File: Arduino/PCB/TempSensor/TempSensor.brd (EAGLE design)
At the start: 32.7 x 32.4 mm, 24 parts, among them IC1 DS1820, J1 FTDI_DEVICE, J2 FTDI_DEVICE, U1 ATMEGA328-AU, X1 16Mhz

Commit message: base board
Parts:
- removed PWR1: IE0503D, xp_power:XP_DIP
- added C10, C4, C5, C6, C7, C8, C9: 100n, rcl:C0805
- added C11: 10n, rcl:C0805
- added D1: RB161M-20TR, Components:SOD123
- added D2: BAT54HT1G, Components:SOD323_ST
- added L1: VLCF4020, Components:VLCF4020
- added R10, R11, R13, R9: 4k7, rcl:R0805
- added R8: 10k, rcl:R0805
- added U$1: LM2736X, Components:SOT23-6L
- added U$3: XC6210, Components:SOT23-5
- U$2: value OLED_0.96_I2C -> OLED_0.96_I2CSWITCHPOWER
- moved JP5 1.42 mm to (58.4, 51.4)
- moved JP4 0.90 mm to (52.7, 51.4)
- moved JP6 0.71 mm to (44.1, 51.4)
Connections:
- removed net VCC: J2.P$5, LED1.A, SJ2.1, U$2.VCC, U1.18, U1.4, U1.6
- new net N$19: C4.2, D2.C, U$1.1
- new net N$25: R8.1, U$1.4
- new net N$26: C9.2, IC1.3, R11.1
- new net N$27: C10.2, IC1.2, R13.1
- new net N$29: C11.2, U$3.4
- new net VIN: JP6.2, R8.2, U$1.5
- new net VO: C5.2, D2.A, L1.P$2, R9.2, U$3.1, U$3.3
- net +3V3: now also C6.2, C7.2, C8.2, J2.P$5, LED1.A, R11.2, SJ2.1, U$2.GND, U$3.5, U1.18, U1.4, U1.6; no longer IC1.3, PWR1.+VOUT
- net GND: now also C10.1, C11.1, C5.1, C6.1, C7.1, C8.1, C9.1, D1.A, JP6.1, R10.1, U$1.2, U$2.VCC, U$3.2; no longer PWR1.-VOUT, U$2.GND
- net N$11: now also C4.1, D1.C, L1.P$1, U$1.6; no longer JP6.2, PWR1.+VIN
- net N$14: now also R10.2, R9.1, U$1.3; no longer JP6.1, PWR1.-VIN
- net N$6: now also R13.2; no longer IC1.2
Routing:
- net GND: track 85.6 -> 1.86 mm, vias 1 -> 0
- net VCC: track 63.6 -> 0.00 mm
- net +3V3: track 62.0 -> 0.00 mm, vias 1 -> 0
- net N$20: track 54.6 -> 0.00 mm
- net N$10: track 53.3 -> 0.00 mm, vias 1 -> 0
- net N$18: track 44.2 -> 0.00 mm
- net N$6: track 39.2 -> 0.00 mm, vias 1 -> 0
- net N$5: track 36.7 -> 0.00 mm
- net N$12: track 36.3 -> 0.00 mm, vias 1 -> 0
- net N$13: track 32.8 -> 0.00 mm, vias 1 -> 0
- net N$16: track 26.0 -> 0.00 mm, vias 1 -> 0
- net N$8: track 23.4 -> 0.00 mm, vias 1 -> 0
- net N$9: track 23.2 -> 0.00 mm, vias 1 -> 0
- net N$4: track 21.8 -> 0.00 mm
- net N$3: track 17.2 -> 0.00 mm
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
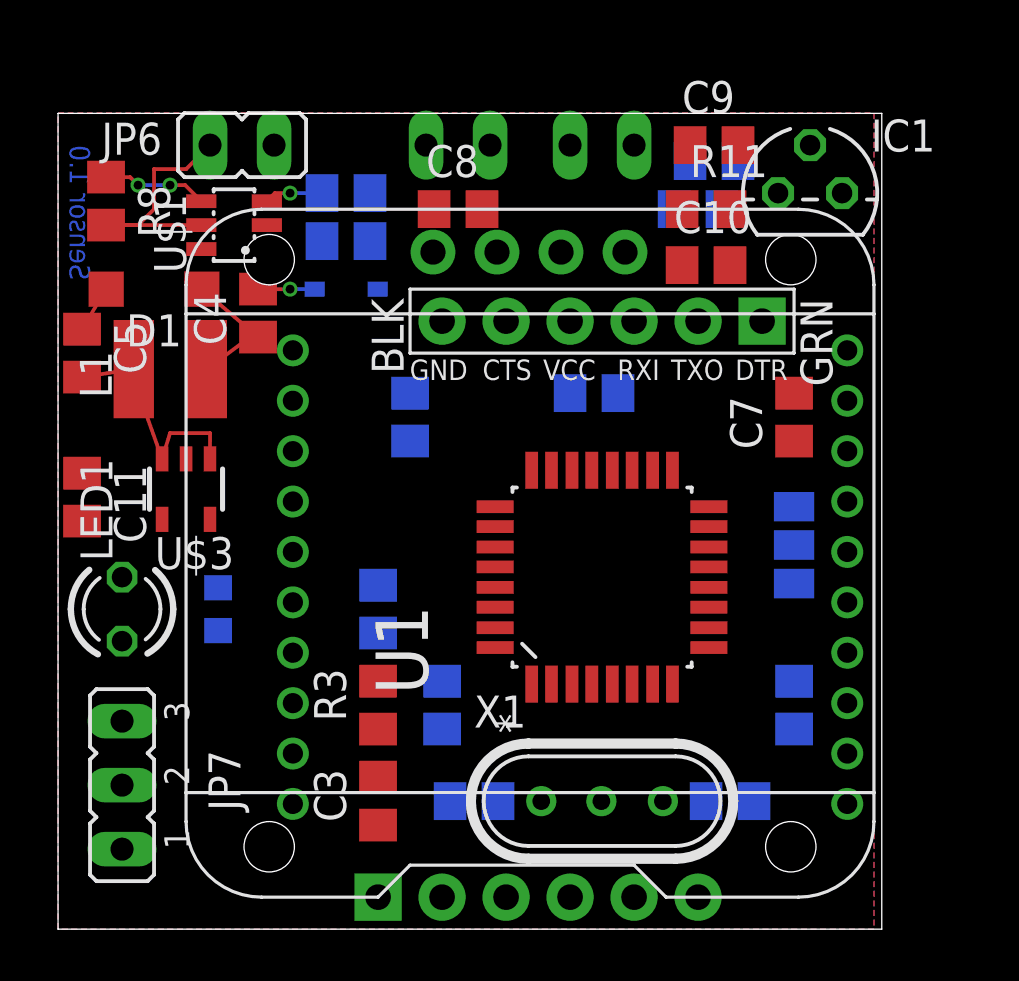
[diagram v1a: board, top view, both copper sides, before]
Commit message: Voor aanpassing board (verplaatsen toetsen en xbee)
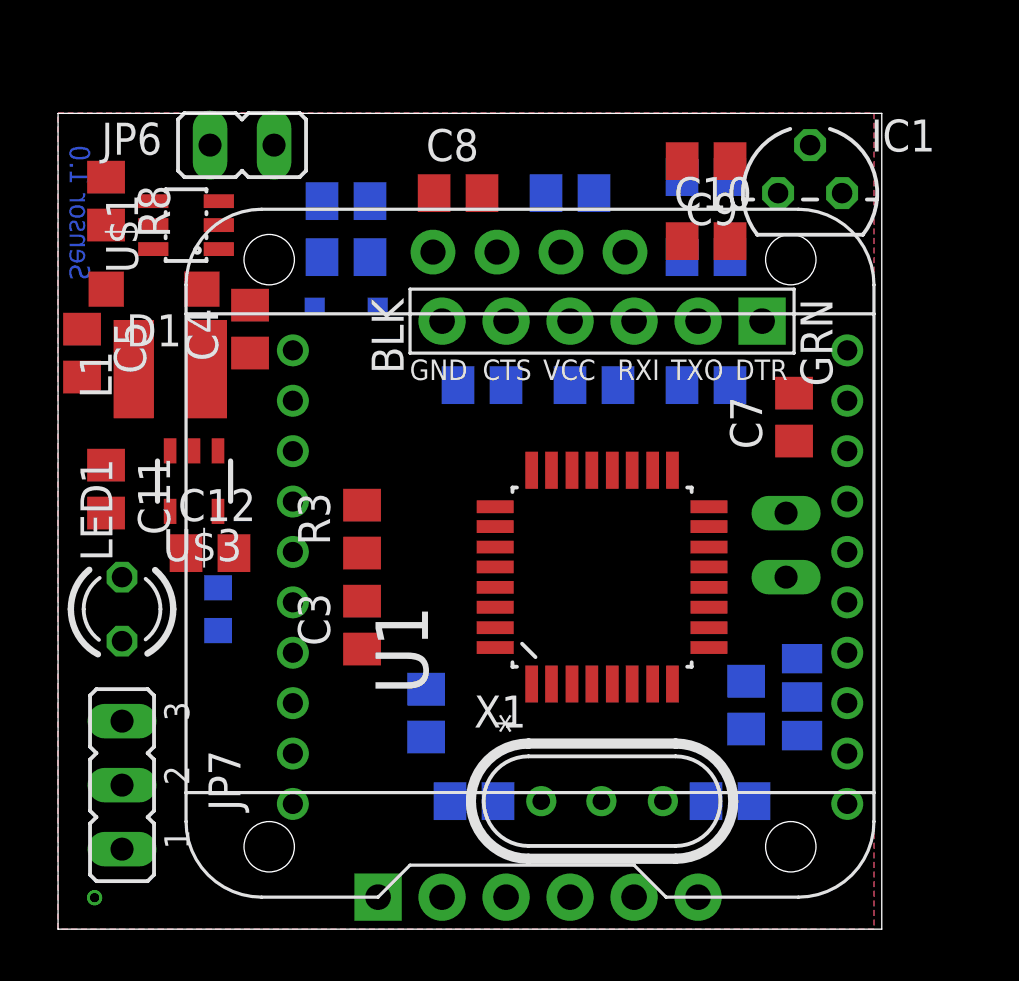
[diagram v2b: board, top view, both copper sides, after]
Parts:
- removed JP4: (no value), jumper:JP1
- added C12: 1u, rcl:C0805
- R10: value 4k7 -> 21K5
- R11, R13: value 4k7 -> 560
- R6, R7: value 4k7 -> 1M
- R9: value 4k7 -> 10K
- moved JP5 17.5 mm to (65.7, 35.6), turned to 180 degrees
- moved R1 15.8 mm to (62.5, 41.9), turned to 0 degrees
- moved R4 7.41 mm to (58.1, 41.9), turned to 0 degrees
- moved C3 7.01 mm to (48.9, 32.4)
- moved R3 7.01 mm to (48.9, 36.2)
- moved SJ2 6.04 mm to (66.4, 29.5)
- moved R5 5.12 mm to (57.1, 49.5), turned to 0 degrees
- moved C6 4.46 mm to (53.7, 41.9)
- moved R13 3.82 mm to (62.5, 47.0)
- moved R7 1.91 mm to (64.1, 29.2)
- moved U$1 1.91 mm to (41.9, 48.3)
- moved R11 1.27 mm to (62.5, 50.2), flipped to the bottom, turned to 180 degrees
- moved C11 1.00 mm to (38.7, 37.8)
- moved C10 0.95 mm to (62.5, 47.6)
- moved C9 0.71 mm to (62.5, 50.8), turned to 180 degrees
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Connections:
- net +3V3: now also C12.2
- net GND: now also C12.1
- net N$10: no longer JP4.1, JP5.1
- net N$12: now also JP5.1; no longer JP4.2
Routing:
- net VO: track 9.69 -> 0.00 mm
- net VIN: track 9.52 -> 0.00 mm
- net N$11: track 5.38 -> 0.00 mm
- net N$25: track 4.17 -> 0.00 mm, vias 2 -> 0
- net N$19: track 3.90 -> 0.00 mm, vias 1 -> 0
- net N$14: track 2.33 -> 0.00 mm, vias 1 -> 0
- net GND: track 1.86 -> 0.00 mm

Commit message: met manuele routing power
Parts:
- moved R7 8.08 mm to (58.4, 34.9), turned to 0 degrees
- moved R6 7.96 mm to (58.4, 32.7), turned to 0 degrees
- moved D2 6.36 mm to (41.9, 45.4), turned to 0 degrees
- moved R10 6.36 mm to (41.9, 47.3), turned to 180 degrees
- moved R9 6.35 mm to (41.9, 49.2), turned to 0 degrees
- moved JP6 5.08 mm to (39.1, 51.4), flipped to the bottom, turned to 270 degrees
- moved U$2 3.51 mm to (55.6, 39.1)
- moved XB1 2.54 mm to (57.1, 36.8)
- moved C12 2.25 mm to (43.2, 33.0), turned to 90 degrees
- moved C8 2.13 mm to (51.8, 47.6)
- moved R5 2.01 mm to (56.5, 47.6)
- moved J2 1.93 mm to (56.5, 44.8)
- moved IC1 1.71 mm to (68.3, 48.9), turned to 90 degrees
- moved SJ2 1.59 mm to (64.8, 29.5), turned to 180 degrees
- moved U$3 1.35 mm to (43.2, 37.1)
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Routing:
- net VO: track 0.00 -> 16.5 mm, vias 0 -> 1

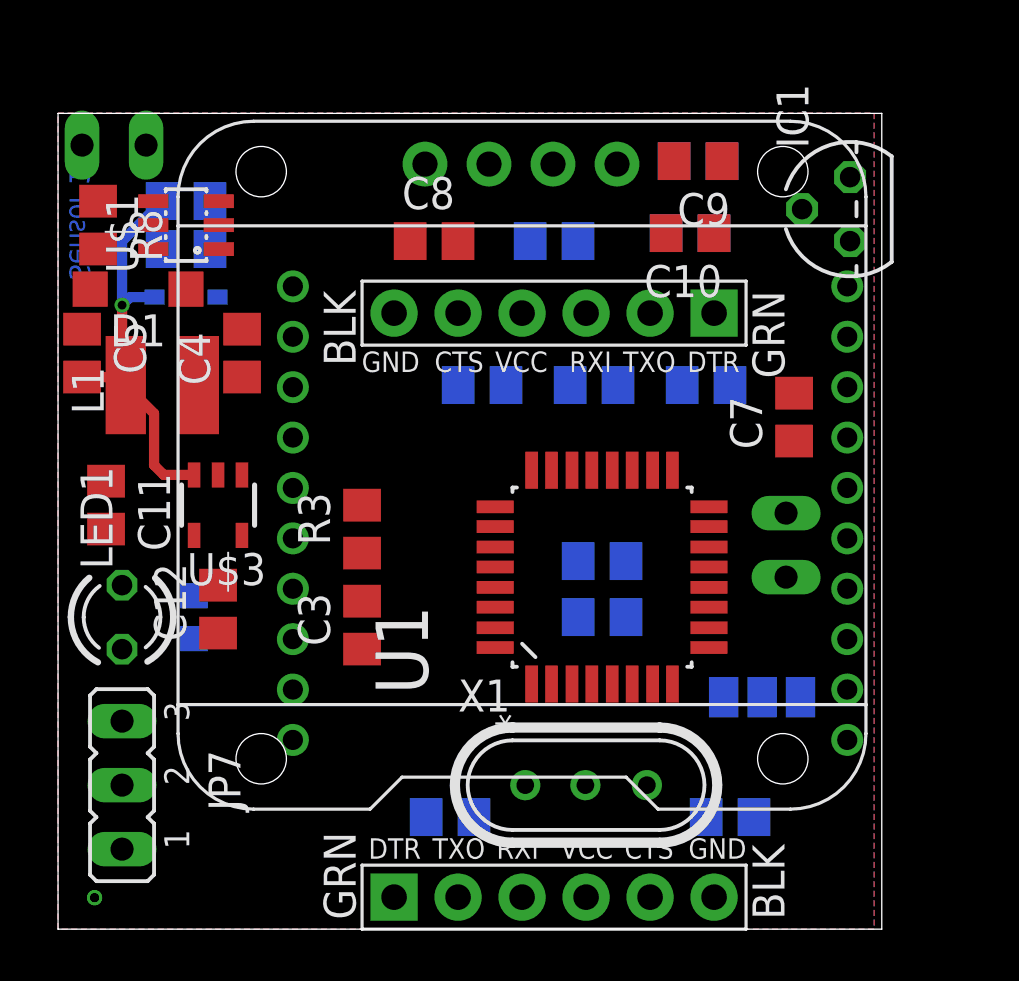
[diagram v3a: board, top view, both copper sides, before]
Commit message: xbee/oled positie + power routed
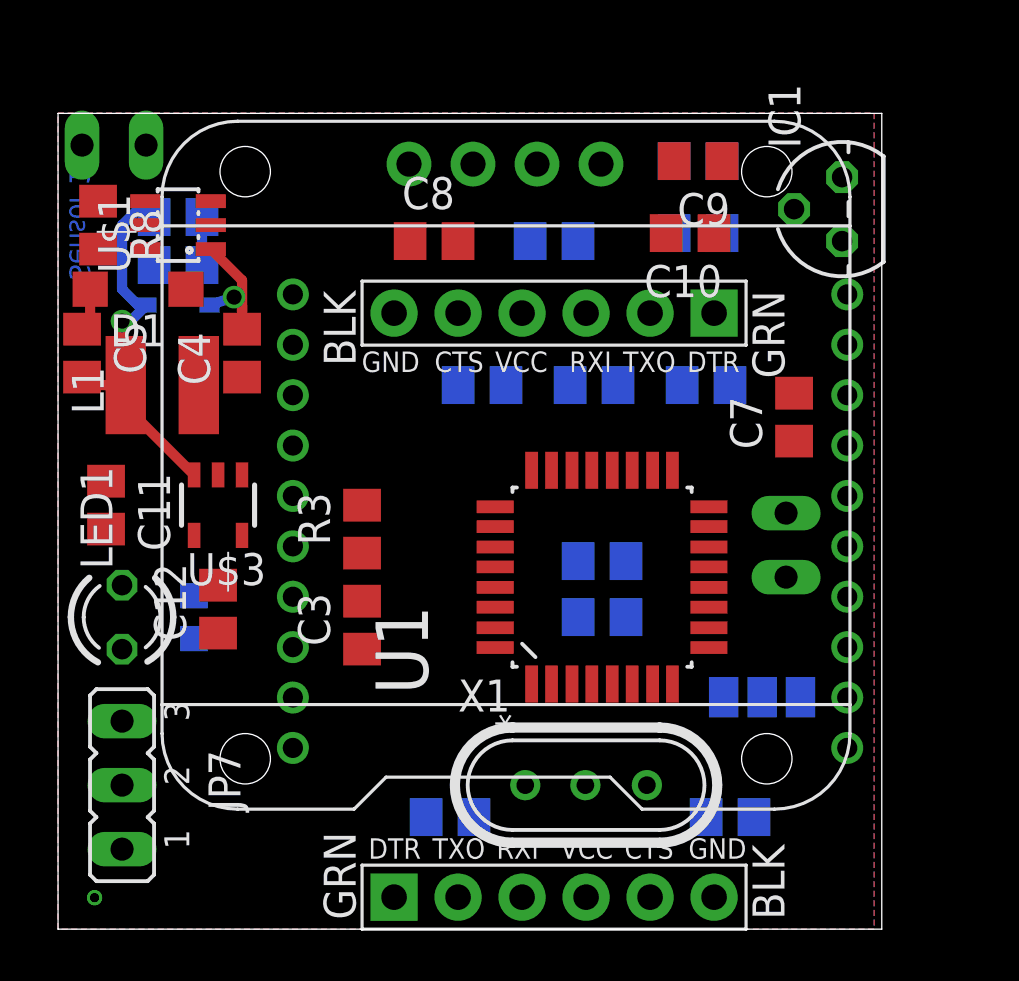
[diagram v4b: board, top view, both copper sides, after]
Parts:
- moved R10 0.71 mm to (41.6, 46.7)
- moved R9 0.71 mm to (41.6, 48.6)
- moved U$2 0.63 mm to (54.9, 39.1)
- moved D2 0.45 mm to (41.6, 45.1)
- moved IC1 0.32 mm to (67.9, 48.9)
- moved R13 0.32 mm to (62.2, 47.9)
- moved U$1 0.32 mm to (41.6, 48.3)
- moved XB1 0.32 mm to (57.1, 36.5)
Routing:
- net N$19: track 0.00 -> 6.12 mm, vias 0 -> 1
- net N$14: track 0.00 -> 1.91 mm
- net GND: track 0.00 -> 1.72 mm
- net VO: track 16.5 -> 15.2 mm

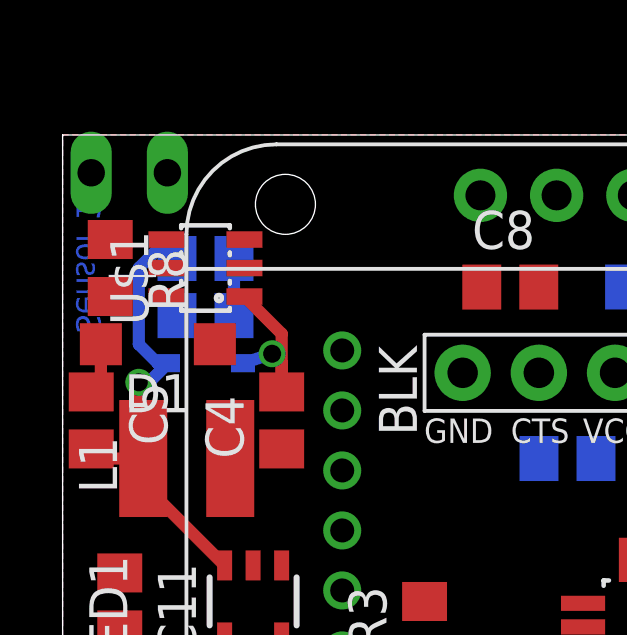
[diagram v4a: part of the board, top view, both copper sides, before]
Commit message: power routed
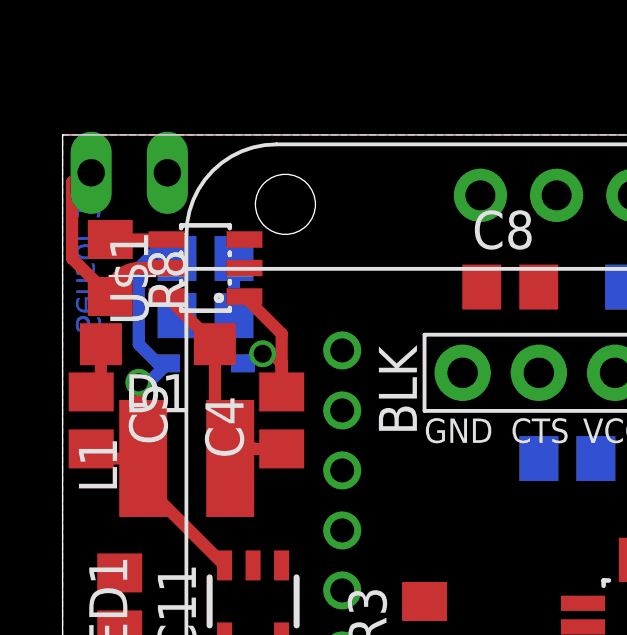
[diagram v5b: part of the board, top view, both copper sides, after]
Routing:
- net VIN: track 0.00 -> 7.37 mm
- net N$11: track 0.00 -> 7.24 mm
- net N$25: track 0.00 -> 1.88 mm
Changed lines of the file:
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@@
 <contactref element="U$1" pad="5"/>
 <contactref element="R8" pad="2"/>
-<wire x1="38.4175" y1="47.31" x2="37.7825" y2="51.435" width="0" layer="19" extent="1-1"/>
-<wire x1="40.2925" y1="48.26" x2="38.4175" y2="47.31" width="0" layer="19" extent="1-1"/>
+<wire x1="38.4175" y1="47.31" x2="37.15" y2="48.5775" width="0.4064" layer="1"/>
+<wire x1="37.15" y1="48.5775" x2="37.1475" y2="48.5775" width="0.4064" layer="1"/>
+<wire x1="37.1475" y1="48.5775" x2="37.1475" y2="51.1175" width="0.4064" layer="1"/>
+<wire x1="37.1475" y1="51.1175" x2="37.465" y2="51.435" width="0.4064" layer="1"/>
+<wire x1="37.465" y1="51.435" x2="37.7825" y2="51.435" width="0.4064" layer="1"/>
+<wire x1="40.2925" y1="48.26" x2="40.005" y2="48.26" width="0.4064" layer="1"/>
+<wire x1="40.005" y1="48.26" x2="39.3675" y2="48.26" width="0.4064" layer="1"/>
+<wire x1="39.3675" y1="48.26" x2="38.4175" y2="47.31" width="0.4064" layer="1" curve="90"/>
 </signal>
 <signal name="N$19" class="1">
@@
 <wire x1="44.1325" y1="44.13" x2="44.1325" y2="45.085" width="0.4064" layer="1"/>
 <wire x1="44.1325" y1="45.085" x2="43.815" y2="45.4025" width="0.4064" layer="1"/>
-<via x="43.815" y="45.4025" extent="1-16" drill="0.6" shape="square"/>
-<wire x1="43.815" y1="45.4025" x2="42.8425" y2="45.085" width="0.4064" layer="16"/>
+<wire x1="43.815" y1="45.4025" x2="43.4975" y2="45.4025" width="0.4064" layer="1"/>
+<via x="43.4975" y="45.4025" extent="1-16" drill="0.6" shape="square"/>
+<wire x1="43.4975" y1="45.4025" x2="42.8425" y2="45.085" width="0.4064" layer="16"/>
 </signal>
 <signal name="N$25">
 <contactref element="R8" pad="1"/>
 <contactref element="U$1" pad="4"/>
-<wire x1="40.2925" y1="49.21" x2="38.4175" y2="49.21" width="0" layer="19" extent="1-1"/>
+<wire x1="38.4175" y1="49.21" x2="40.2925" y2="49.21" width="0.4064" layer="1"/>
 </signal>
 <signal name="N$26">
@@
 <contactref element="L1" pad="P$1"/>
 <contactref element="D1" pad="C"/>
-<wire x1="40.2925" y1="47.31" x2="41.905" y2="45.72" width="0" layer="19" extent="1-1"/>
-<wire x1="42.4175" y1="41.91" x2="41.905" y2="45.72" width="0" layer="19" extent="1-1"/>
-<wire x1="44.1325" y1="42.23" x2="42.4175" y2="41.91" width="0" layer="19" extent="1-1"/>
+<wire x1="40.2925" y1="47.31" x2="41.905" y2="45.72" width="0.4064" layer="1"/>
+<wire x1="41.905" y1="45.72" x2="41.91" y2="45.715" width="0.4064" layer="1"/>
+<wire x1="41.91" y1="45.715" x2="41.91" y2="43.4975" width="0.4064" layer="1"/>
+<wire x1="41.91" y1="43.4975" x2="43.1775" y2="42.23" width="0.4064" layer="1"/>
+<wire x1="43.1775" y1="42.23" x2="44.1325" y2="42.23" width="0.4064" layer="1"/>
+<wire x1="43.1775" y1="42.23" x2="42.4175" y2="41.91" width="0" layer="19" extent="1-1"/>
 </signal>
 <signal name="N$14">
@@
 <contactref element="R10" pad="2"/>
 <contactref element="U$1" pad="3"/>
+<wire x1="42.5425" y1="48.5775" x2="42.5425" y2="46.6725" width="0.4064" layer="16"/>
 <wire x1="42.5425" y1="48.5775" x2="42.8925" y2="49.21" width="0" layer="19" extent="1-16"/>
-<wire x1="42.5425" y1="48.5775" x2="42.5425" y2="46.6725" width="0.4064" layer="16"/>
 </signal>
 <signal name="GND2" class="1">

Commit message: power routed/ labels placed
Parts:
- renumbered U$1 to U2, U$3 to U3
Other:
- board size 32.7 x 32.4 mm -> 32.7 x 32.7 mm
